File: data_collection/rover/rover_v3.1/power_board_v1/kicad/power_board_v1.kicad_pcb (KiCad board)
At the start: 2 copper layers, 90 x 65 mm, 100 parts, among them J1 XT60_BATT, J10 from Pi USB2, J11 UPDI prog (UPDI/3V3/GND), J12 XT30 fallback pads, J2 PANEL_SW, J3 USB4105-GF-A (TH shell), J4 USB_A radio1, J5 USB_A radio2, J6 AUX 5V 2A, J7 PI GPIO harness, J8 AUX_CTL out (JST-GH), J9 from Pi USB1, Q2 CSD18543Q3A diode, Q3 CSD18543Q3A switch, U1 LM5145 5.1V rail A, U2 LM5145 5.1V rail B, U3 ATtiny816 (VQFN), U4 LM74800-Q1, U5 INA226 (addr 0x40), U6 TPS7A1633 3V3 60V LDO, U7 TPS2553 1.7A, U8 TPS2553 1.7A, U9 AP2112K-3.3 (switched)

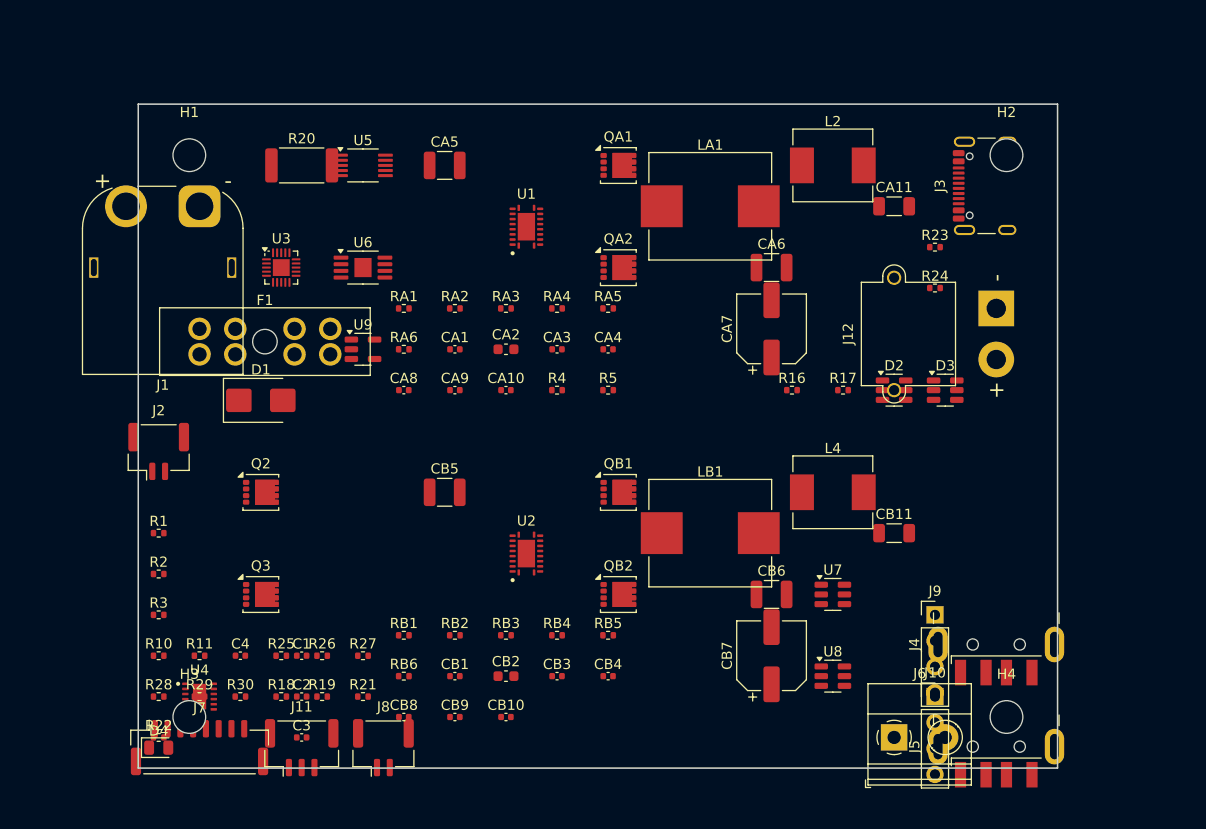
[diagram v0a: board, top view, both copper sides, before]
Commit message: P4 placement pass: measured-bbox anchor map + greedy overlap resolver -> 0 bbox overlaps; GND pours both layers (thermal reliefs); JLC design rules; headless DRC via pcbnew.WriteDRCReport wired into generator
Co-Authored-By: Claude Fable 5 <noreply@anthropic.com>
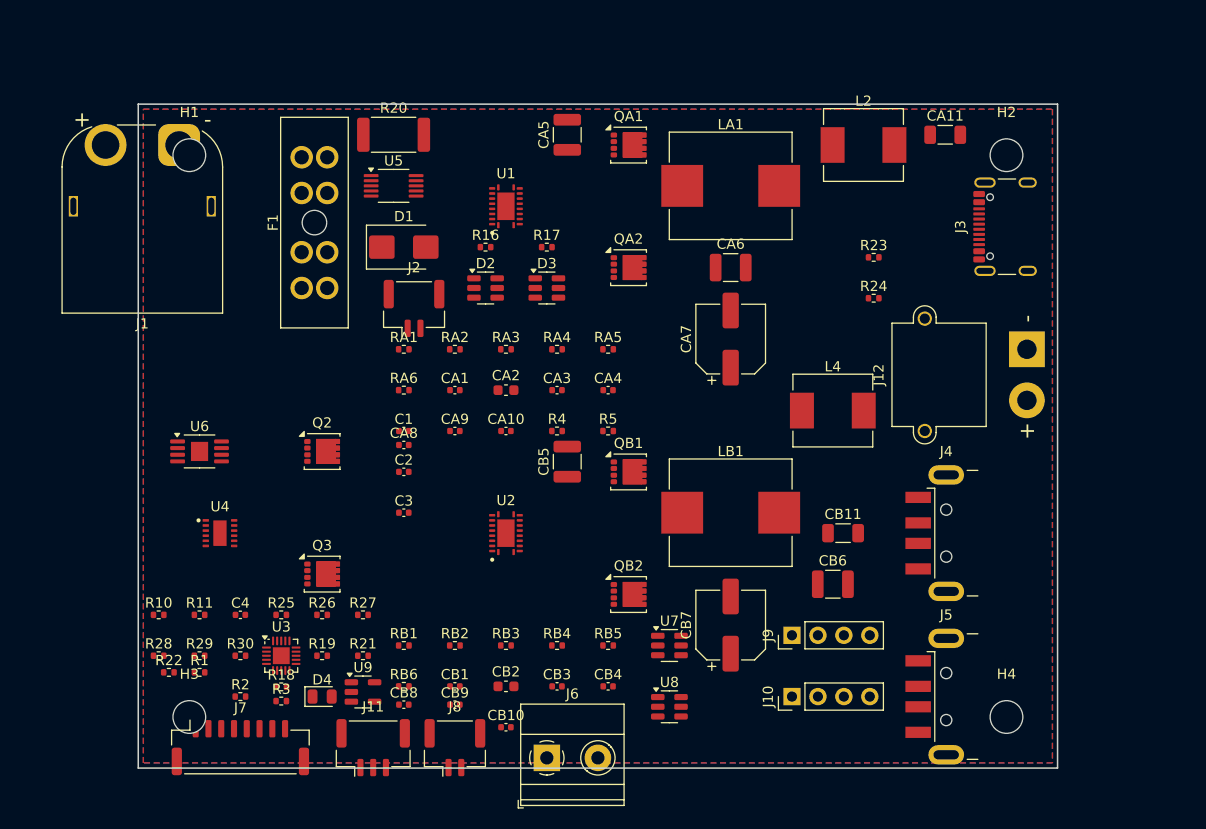
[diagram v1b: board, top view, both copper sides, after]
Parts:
- moved D2 41.2 mm to (84.0, 68.0)
- moved D3 40.3 mm to (90.0, 68.0)
- moved U3 38.0 mm to (64.0, 104.0)
- moved J6 34.1 mm to (90.0, 114.0)
- moved U9 33.5 mm to (72.0, 107.5)
- moved R16 33.1 mm to (84.0, 64.0)
- moved R17 32.2 mm to (90.0, 64.0)
- moved J2 28.7 mm to (77.0, 70.0)
- moved C1 24.2 mm to (76.0, 82.0)
- moved C2 24.2 mm to (76.0, 86.0)
- moved C3 24.2 mm to (76.0, 90.0)
- moved U6 24.1 mm to (56.0, 84.0)
- moved D1 20.5 mm to (76.0, 64.0)
- moved D4 16.8 mm to (68.0, 108.0)
- moved U7 16.8 mm to (102.0, 103.0)
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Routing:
- added copper zone on B.Cu, net GND
- added copper zone on F.Cu, net GND

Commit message: P4 placement fixes from review: XT60 pads were 3.2mm off-board (rot/origin confusion) -> pads on copper, shroud overhangs; J1 pad no longer collides corner mounting hole; J12 mate faces off right edge; bottom connectors raised off edge; 0 overlaps
Co-Authored-By: Claude Fable 5 <noreply@anthropic.com>
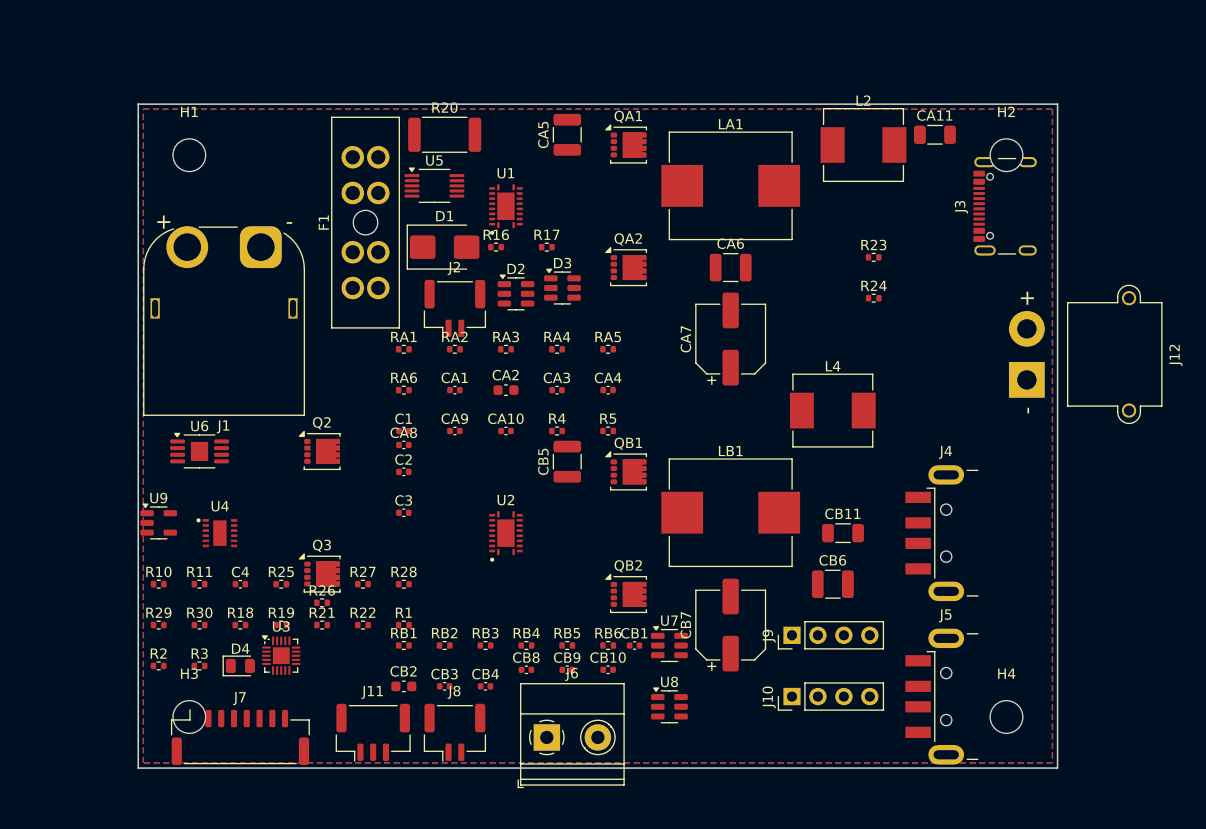
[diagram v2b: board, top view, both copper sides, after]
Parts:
- moved U9 26.0 mm to (52.0, 91.0)
- moved R28 25.0 mm to (76.0, 97.0)
- moved R1 20.5 mm to (76.0, 101.0)
- moved RB6 20.4 mm to (96.0, 103.0)
- moved R22 19.6 mm to (72.0, 101.0)
- moved CB1 18.0 mm to (98.6, 103.0)
- moved J1 12.8 mm to (62.0, 64.0)
- moved CB8 12.5 mm to (88.0, 105.4)
- moved CB4 12.0 mm to (84.0, 107.0)
- moved CB9 11.5 mm to (92.0, 105.4)
- moved CB10 11.5 mm to (96.0, 105.4)
- moved CB3 11.0 mm to (80.0, 107.0)
- moved CB2 10.0 mm to (76.0, 107.0)
- moved R3 8.71 mm to (56.0, 105.0)
- moved D4 8.54 mm to (60.0, 105.0)
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
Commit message: Adversarial review response: schematic v4 (decoupling C5-C17+CE1, split bulk caps ->127 comps, 3V3_SW pulls, PGOOD seq divider fixes INA226 abs-max + bootstrap deadlock, rail-A sense/setpoint, wc RILIM, aux polyfuse, 5V TVS, rev-batt schottky, FE_EN delay); firmware boot-glitch + cold-on fixes (11 tests green); board re-floorplan (J1/J12/J3 orientations, monotonic power corridor, tight hot loops, refill-after-resolve, solid pours + 20 thermal vias); REVIEW_FINDINGS.md disposition
Co-Authored-By: Claude Fable 5 <noreply@anthropic.com>
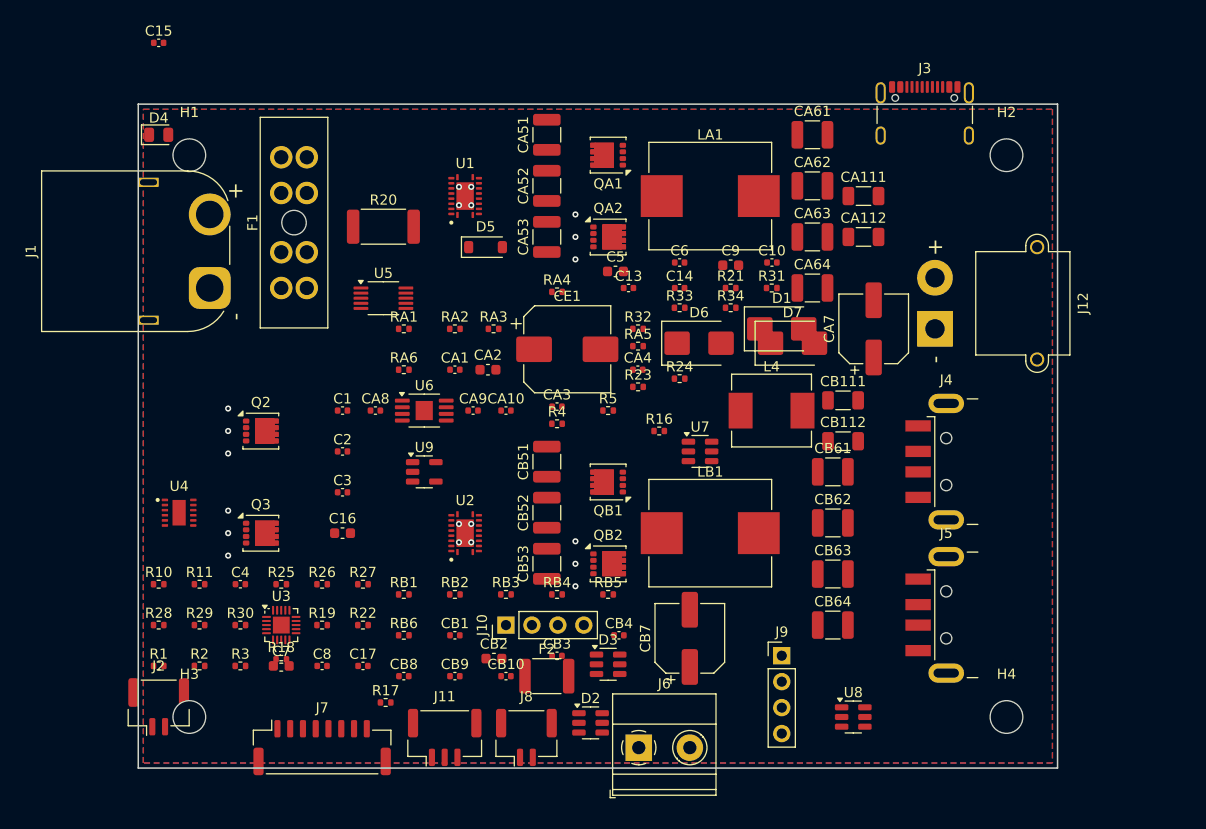
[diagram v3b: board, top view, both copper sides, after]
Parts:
- removed CA11, CB11: 2x22u pi-out, C_1206_3216Metric
- removed CA5, CB5: 3x10u 50V in, C_1210_3225Metric
- removed CA6, CB6: 4x47u 10V out, C_1210_3225Metric
- removed L2: pi-filter 1u, L_Chilisin_BMRx00060630
- added C10: 100n INA vs, C_0402_1005Metric, F.Cu at (112.0, 65.5)
- added C13: 100n U7 in, C_0402_1005Metric, F.Cu at (98.0, 68.0)
- added C14: 100n U8 in, C_0402_1005Metric, F.Cu at (103.0, 68.0)
- added C15: 100n at U4.A, C_0402_1005Metric, F.Cu at (52.0, 44.0)
- added C16: 2u2 EN delay, C_0603_1608Metric, F.Cu at (70.0, 92.0)
- added C17: 100n sw debounce, C_0402_1005Metric, F.Cu at (72.0, 105.0)
- added C5: 1u LDO in, C_0603_1608Metric, F.Cu at (96.7, 66.4)
- added C6: 100n LDO in, C_0402_1005Metric, F.Cu at (103.0, 65.5)
- added C7: 2u2 LDO out, C_0603_1608Metric, F.Cu at (64.0, 105.0)
- added C8: 100n MCU vdd, C_0402_1005Metric, F.Cu at (68.0, 105.0)
- added C9: 1u LDO out, C_0603_1608Metric, F.Cu at (108.0, 65.8)
- added CA111: 22u local, C_1206_3216Metric, F.Cu at (121.0, 59.0)
- added CA112: 22u local, C_1206_3216Metric, F.Cu at (121.0, 63.0)
- added CA51: 10u 50V X7R, C_1210_3225Metric, F.Cu at (90.0, 53.0)
- added CA52: 10u 50V X7R, C_1210_3225Metric, F.Cu at (90.0, 58.0)
- added CA53: 10u 50V X7R, C_1210_3225Metric, F.Cu at (90.0, 63.0)
- added CA61: 47u 10V X7R, C_1210_3225Metric, F.Cu at (116.0, 53.0)
- added CA62: 47u 10V X7R, C_1210_3225Metric, F.Cu at (116.0, 58.0)
- added CA63: 47u 10V X7R, C_1210_3225Metric, F.Cu at (116.0, 63.0)
- added CA64: 47u 10V X7R, C_1210_3225Metric, F.Cu at (116.0, 68.0)
- added CB111: 22u pi-out, C_1206_3216Metric, F.Cu at (119.0, 79.0)
- added CB112: 22u pi-out, C_1206_3216Metric, F.Cu at (119.0, 83.0)
- added CB51: 10u 50V X7R, C_1210_3225Metric, F.Cu at (90.0, 85.0)
- added CB52: 10u 50V X7R, C_1210_3225Metric, F.Cu at (90.0, 90.0)
- added CB53: 10u 50V X7R, C_1210_3225Metric, F.Cu at (90.0, 95.0)
- added CB61: 47u 10V X7R, C_1210_3225Metric, F.Cu at (118.0, 86.0)
- added CB62: 47u 10V X7R, C_1210_3225Metric, F.Cu at (118.0, 91.0)
- added CB63: 47u 10V X7R, C_1210_3225Metric, F.Cu at (118.0, 96.0)
- added CB64: 47u 10V X7R, C_1210_3225Metric, F.Cu at (118.0, 101.0)
- added CE1: 100u hybrid 25V, CP_Elec_8x10, F.Cu at (92.0, 74.0)
- added D5: B5819W schottky, D_SOD-123, F.Cu at (84.0, 64.0)
- added D6: SMBJ5.0A, D_SMB, F.Cu at (104.9, 73.4)
- added D7: SMBJ5.0A, D_SMB, F.Cu at (114.0, 73.4)
- added F2: 2A polyfuse, Fuse_1812_4532Metric, F.Cu at (90.0, 106.0)
- added R31: 100k EN1 pu (5V_B), R_0402_1005Metric, F.Cu at (112.0, 68.0)
- added R32: 100k EN2 pu (5V_B), R_0402_1005Metric, F.Cu at (98.9, 72.0)
- added R33: 20k seq div hi, R_0402_1005Metric, F.Cu at (103.0, 69.9)
- added R34: 16k5 seq div lo, R_0402_1005Metric, F.Cu at (108.0, 69.9)
- R18, R19: value 4k7 I2C pu -> 4k7 I2C pu (3V3_SW)
- R21: value 10k PGOOD_A pu -> 20k PGOOD_A pu (5V_A)
- R22: value 10k PGOOD_B pu -> 10k PGOOD_B pu (3V3_SW)
- RA2: value 301R RILIM (7A valley) -> 348R RILIM (wc-min 6.3A)
- RA4: value 3k74 RFB2 -> 3k65 RFB2 (5.18V)
- RB2: value 243R RILIM (5.7A valley) -> 261R RILIM (wc-min 4.8A)
- RB4: value 3k74 RFB2 -> 3k74 RFB2 (5.08V)
- U1: value LM5145 5.1V rail A -> LM5145 rail A
- U2: value LM5145 5.1V rail B -> LM5145 rail B
- moved D4 52.6 mm to (52.0, 53.0)
- moved R21 51.9 mm to (108.0, 68.0)
- moved J2 48.6 mm to (52.0, 109.0)
- moved R17 47.3 mm to (74.2, 108.6)
- moved D2 42.6 mm to (94.3, 110.6)
- moved D3 37.1 mm to (96.0, 104.8)
- moved D1 34.0 mm to (113.0, 72.0)
- moved J10 28.9 mm to (86.0, 101.0)
- moved U9 26.5 mm to (78.0, 86.0)
- moved R23 26.3 mm to (98.9, 77.7)
- moved R1 24.3 mm to (52.0, 105.0)
- moved R28 24.3 mm to (52.0, 101.0)
- moved R16 24.1 mm to (101.0, 82.0)
- moved U6 22.4 mm to (78.0, 80.0)
- moved R24 20.6 mm to (103.0, 76.9)
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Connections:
- CA10 pad 1: 5VA_PRE -> 5V_A
- CA7 pad 1: 5VA_PRE -> 5V_A
- J6 pad 1: 5V_B -> AUX_5V
- LA1 pad 2: 5VA_PRE -> 5V_A
- R18 pad 1: MCU_3V3 -> 3V3_SW
- R19 pad 1: MCU_3V3 -> 3V3_SW
- R21 pad 1: MCU_3V3 -> 5V_A
- R21 pad 2: PGOOD_A -> PGOODA_RAW
- R22 pad 1: MCU_3V3 -> 3V3_SW
- RA3 pad 1: 5VA_PRE -> 5V_A
- U1 pad 10: PGOOD_A -> PGOODA_RAW
- U6 pad 5: VBATT_F -> VBATT_FD
- U6 pad 8: VBATT_F -> VBATT_FD
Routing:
- net GND: vias 0 -> 20

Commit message: J1 XT60 moved 4mm south: body now clears H1 M3 screw head by 2.1mm
Co-Authored-By: Claude Fable 5 <noreply@anthropic.com>
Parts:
- moved J1 4.00 mm to (57.0, 72.0)

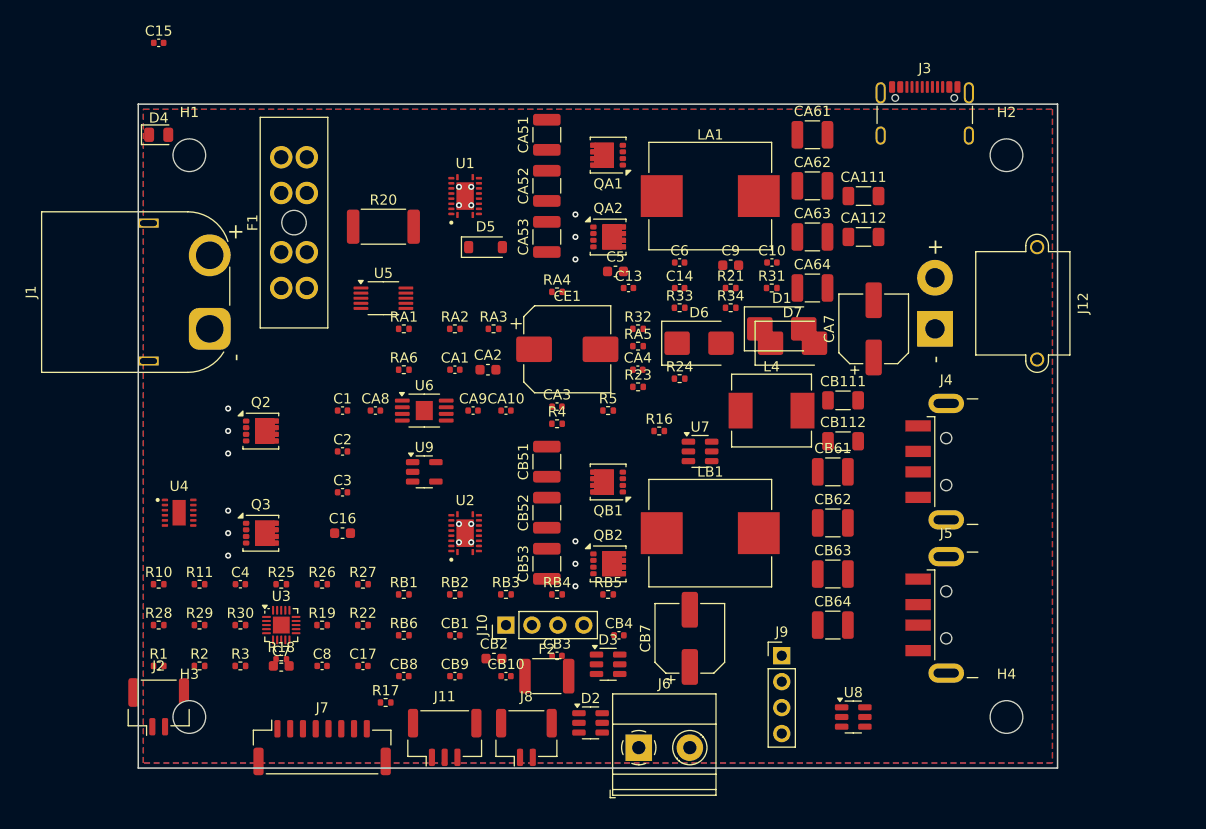
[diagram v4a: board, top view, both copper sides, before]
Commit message: Board revision gate: audit_board.py (I1-I7 invariants incl mate-direction registry + DRC baseline diff) + BOARD_REVISION_CHECKLIST.md; auditor caught+fixed J3 180deg pads-off-board, 11 edge-margin pads, D4/J2 under screw heads; resolver hole keepouts; AUDIT PASS 0 fails
Co-Authored-By: Claude Fable 5 <noreply@anthropic.com>
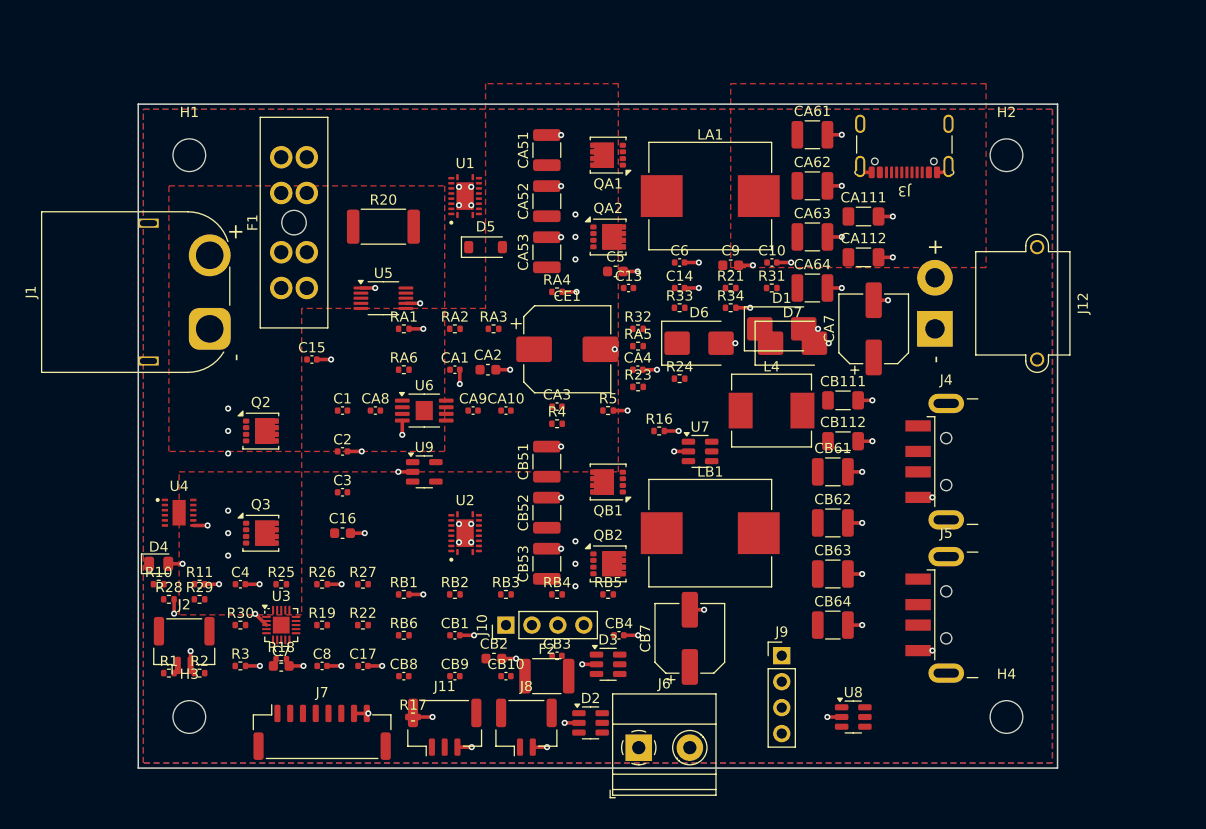
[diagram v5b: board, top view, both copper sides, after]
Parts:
- moved D4 42.0 mm to (52.0, 95.0)
- moved C15 34.4 mm to (67.0, 75.0)
- moved J2 6.50 mm to (54.5, 103.0)
- moved R17 3.03 mm to (76.9, 110.0)
- moved R28 2.71 mm to (53.0, 98.5)
- moved R29 2.52 mm to (56.0, 98.5)
- moved J3 2.24 mm to (125.0, 53.0), turned to 180 degrees
- moved CA111 2.00 mm to (121.0, 61.0)
- moved CA112 2.00 mm to (121.0, 65.0)
- moved CA51 1.50 mm to (90.0, 54.5)
- moved CA52 1.50 mm to (90.0, 59.5)
- moved CA53 1.50 mm to (90.0, 64.5)
- moved J7 1.50 mm to (68.0, 111.5)
- moved R1 1.22 mm to (53.0, 105.7)
- moved J11 1.00 mm to (80.0, 111.0)
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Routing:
- net GND: track 0.00 -> 101.0 mm, vias 20 -> 92
- added copper zone on F.Cu, net 5V_A
- added copper zone on F.Cu, net VBATT_S
- added copper zone on F.Cu, net VSW
